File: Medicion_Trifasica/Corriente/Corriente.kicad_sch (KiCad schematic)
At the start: 0 parts

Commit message: Se agrego el circuito de medicion de corriente
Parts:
- added J1: Conn_01x01_Pin, symbol Connector:Conn_01x01_Pin
- added R1: 22k, symbol Device:R
- added R2: 10k, symbol Device:R
- added U1: ACS725xLCTR-20AB, Package_SO:SOIC-8_3.9x4.9mm_P1.27mm, symbol Sensor_Current:ACS725xLCTR-20AB
- added U2: TL082, symbol Amplifier_Operational:TL082
- added U3: ADR4533, Package_SO:SOIC-8_3.9x4.9mm_P1.27mm, symbol Reference_Voltage:ADR4533
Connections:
- new net: J1.1 (Pin_1), U2.1, U2.2 (-)
- new net: R1.1, U1.7 (VIOUT)
- new net: R1.2, R2.1, U2.3 (+)
- new net: U1.1 (IP+), U1.2 (IP+)
- new net: U1.3 (IP-), U1.4 (IP-)
- new net: U1.8 (VCC), U3.6 (OUT)
- new net +9V: U3.2 (IN)
- new net GND: R2.2, U1.5 (GND), U3.4 (GND)

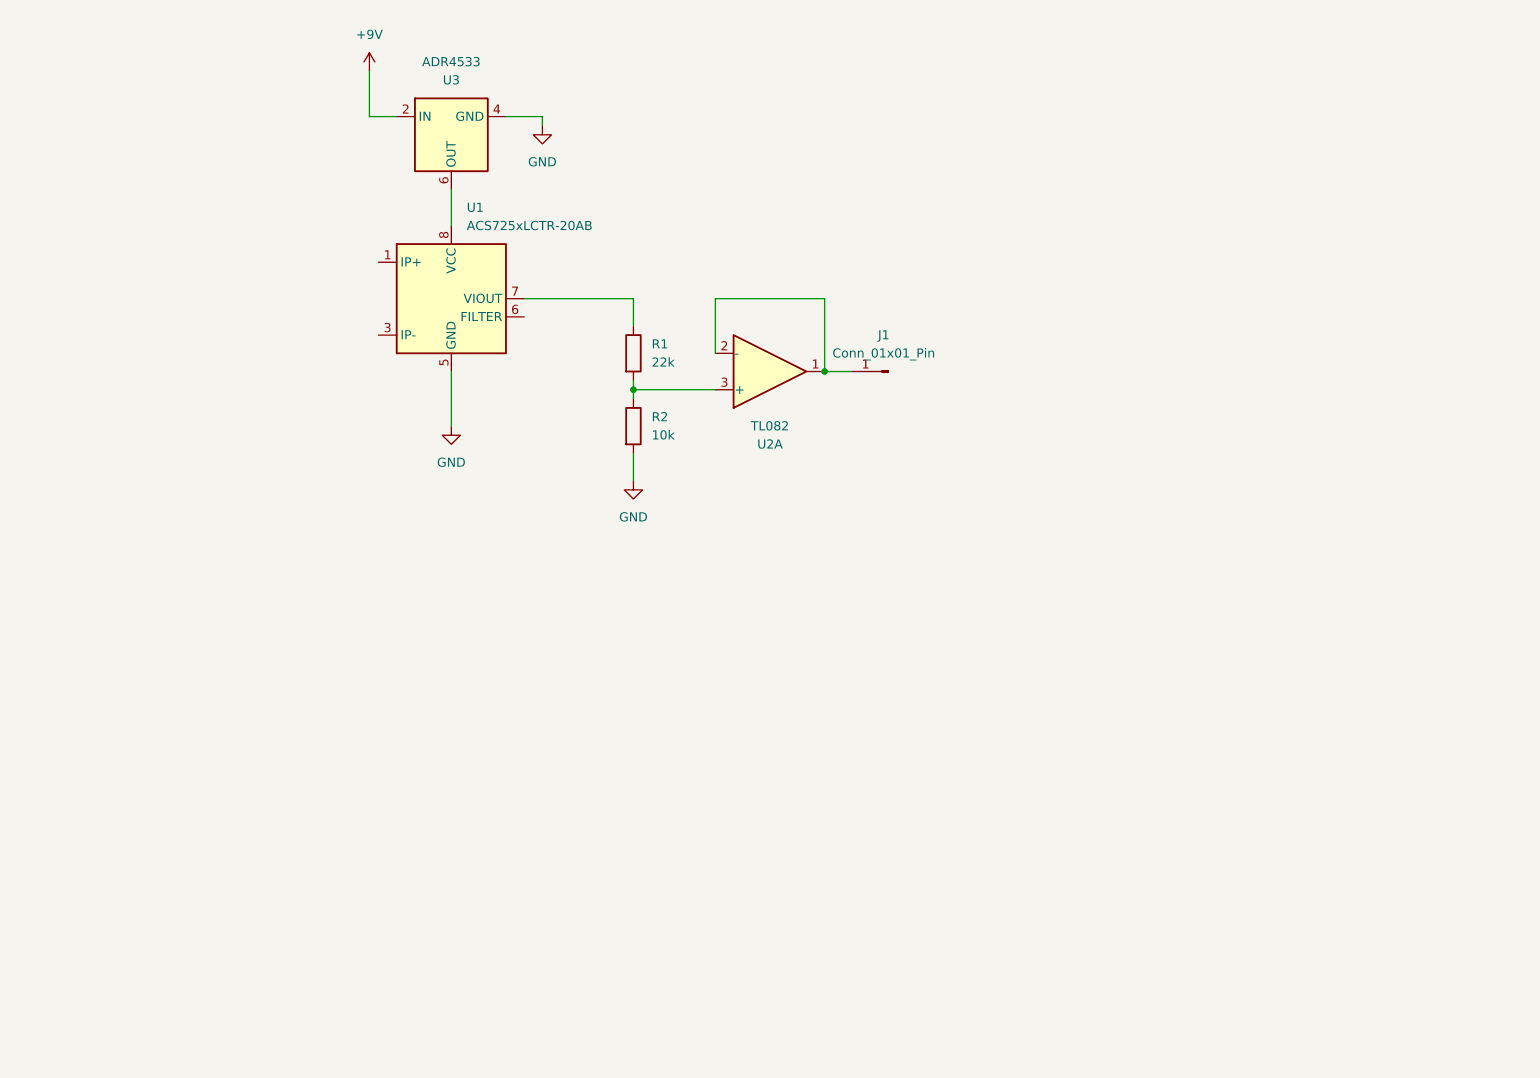
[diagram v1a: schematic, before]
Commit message: Modificaciones finales a los circuitos de medicion de corriente y tension
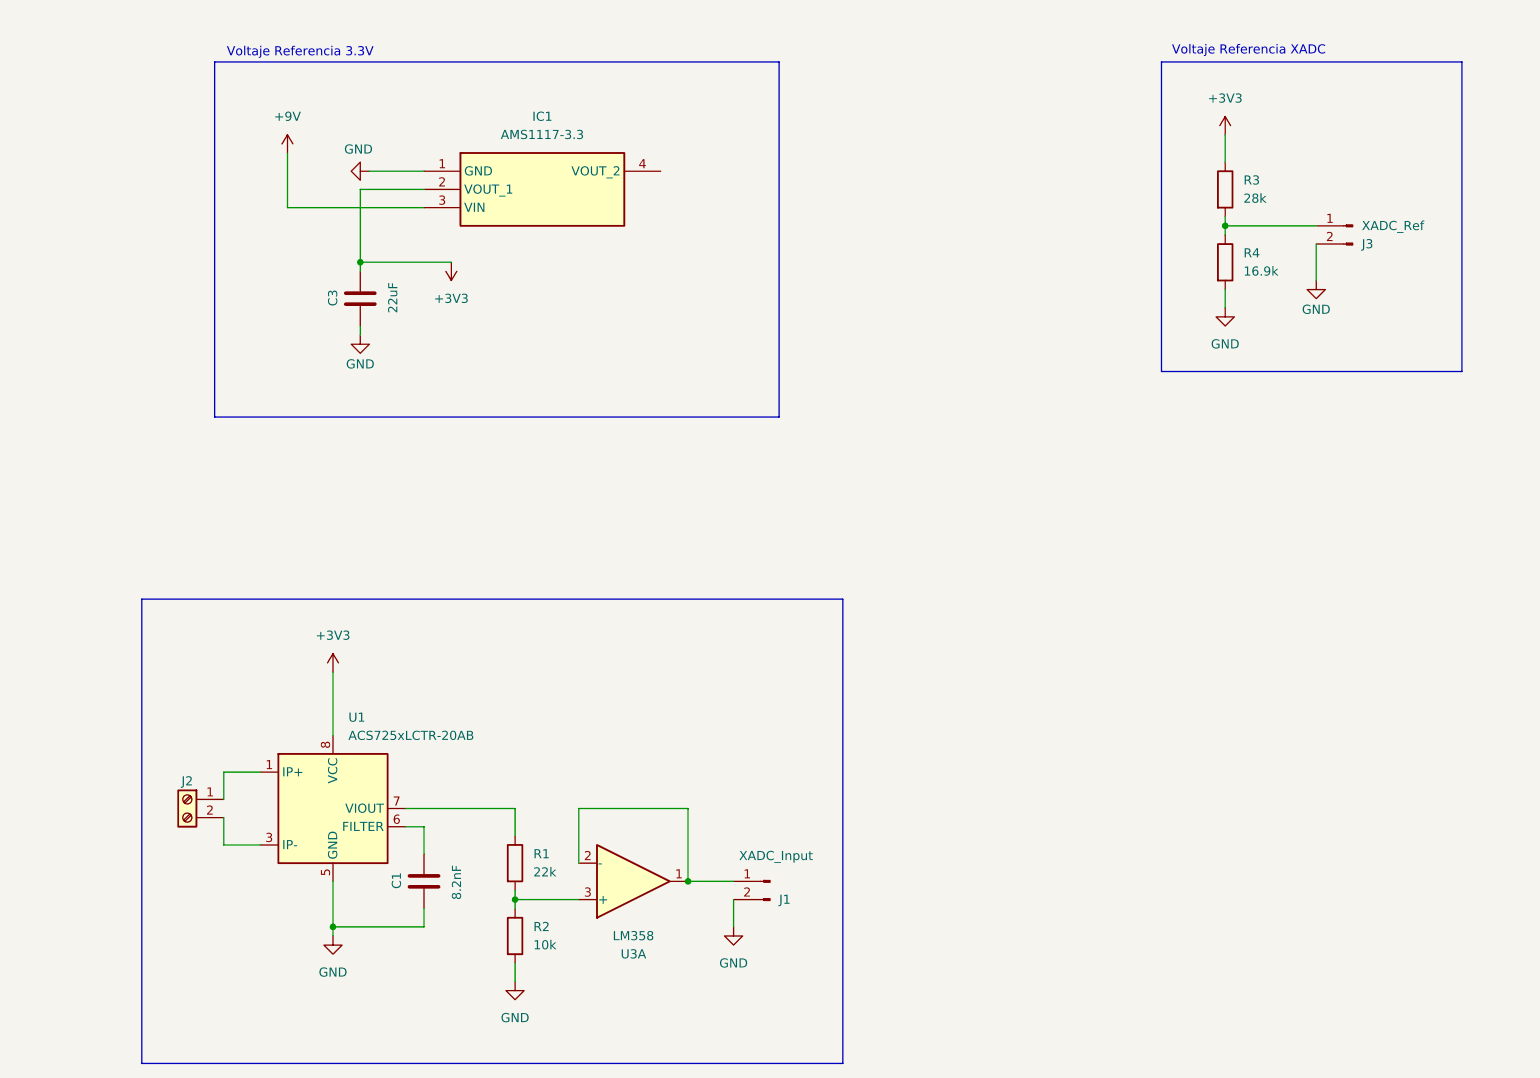
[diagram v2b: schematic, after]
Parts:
- removed J1: Conn_01x01_Pin, symbol Connector:Conn_01x01_Pin
- removed U2: TL082, symbol Amplifier_Operational:TL082
- removed U3: ADR4533, Package_SO:SOIC-8_3.9x4.9mm_P1.27mm, symbol Reference_Voltage:ADR4533
- added C1: 8.2nF, symbol Device:C
- added C3: 22uF, symbol Device:C
- added IC1: AMS1117-3.3, SOT229P700X180-4N, symbol SamacSys_Parts:AMS1117-3.3
- added J1: XADC_Input, symbol Connector:Conn_01x02_Pin
- added J2: Screw_Terminal_01x02, symbol Connector:Screw_Terminal_01x02
- added J3: XADC_Ref, symbol Connector:Conn_01x02_Pin
- added R3: 28k, symbol Device:R
- added R4: 16.9k, symbol Device:R
- added U3: LM358, symbol Amplifier_Operational:LM358
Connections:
- net +9V: now also IC1.3 (VIN)
- net GND: now also C1.1, C3.1, IC1.1 (GND), J1.2 (Pin_2), J3.2 (Pin_2), R4.2
- net at R1.2, R2.1: now also U3.3 (+)
- net at U1.1 (IP+), U1.2 (IP+): now also J2.1 (Pin_1)
- net at U1.3 (IP-), U1.4 (IP-): now also J2.2 (Pin_2)
- net at U1.6 (FILTER): now also C1.2
- net +3V3: now reaches U1.8 (VCC)
- net +3V3: now also C3.2, IC1.2 (VOUT_1), R3.1
- new net: J3.1 (Pin_1), R3.2, R4.1
- new net: J1.1 (Pin_1), U3.1, U3.2 (-)
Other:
- note added: "Voltaje Referencia 3.3V"
- note added: "Voltaje Referencia XADC"
- company: (none) -> U.N.R
- title: (none) -> Medicion de Corriente
- moved on the sheet: R1, R2, U1

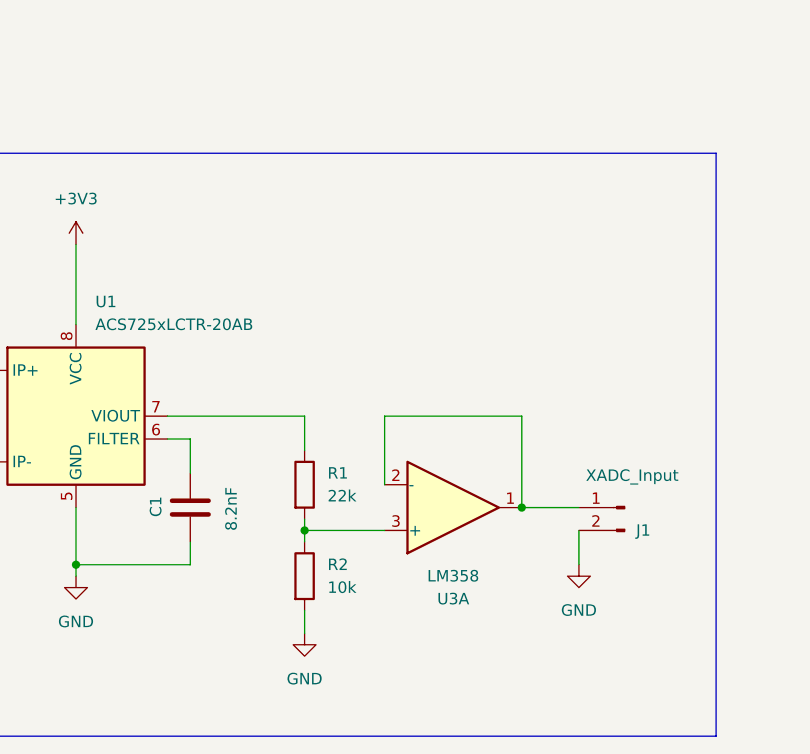
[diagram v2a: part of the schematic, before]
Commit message: Se crearon los esquematicos de los circuitos, y sus footprints
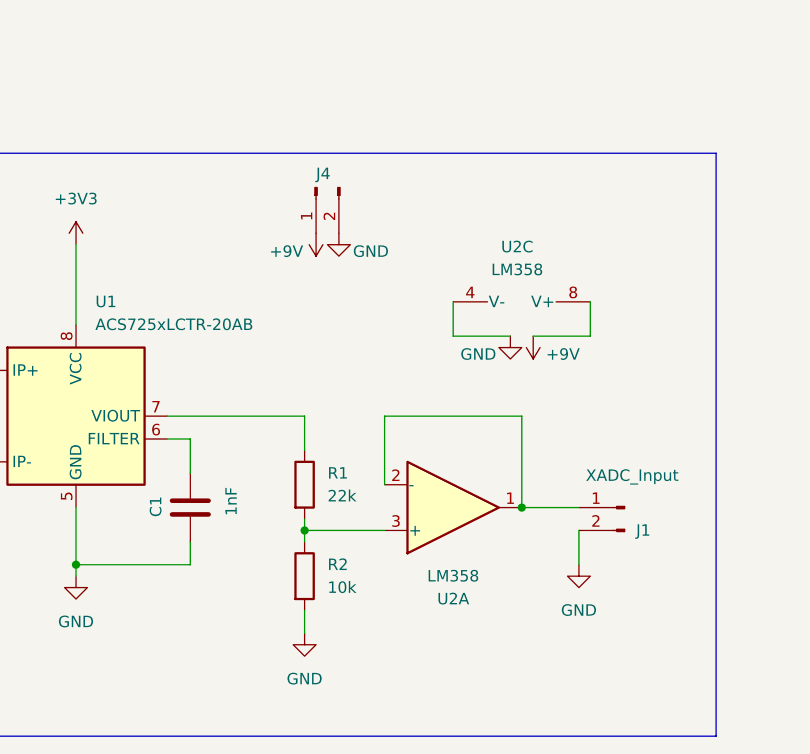
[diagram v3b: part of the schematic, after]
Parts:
- added J4: XADC_Input, Connector_PinHeader_2.54mm:PinHeader_1x02_P2.54mm_Vertical, symbol Connector:Conn_01x02_Pin
- added unit 3 of U2
- C1: value 8.2nF -> 1nF; footprint (none) -> Capacitor_SMD:C_01005_0402Metric_Pad0.57x0.30mm_HandSolder
- C3: footprint (none) -> Capacitor_SMD:C_1206_3216Metric_Pad1.33x1.80mm_HandSolder
- IC1: footprint SOT229P700X180-4N -> SamacSys_Parts:SOT229P700X180-4N
- J1, J3: footprint (none) -> Connector_PinHeader_2.54mm:PinHeader_2x01_P2.54mm_Horizontal
- J2: footprint (none) -> TerminalBlock:TerminalBlock_bornier-2_P5.08mm
- R1, R2, R3, R4: footprint (none) -> Resistor_SMD:R_0805_2012Metric_Pad1.20x1.40mm_HandSolder
- U2: renamed from U3; footprint (none) -> Package_SO:SOIC-8_3.9x4.9mm_P1.27mm
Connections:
- net +9V: now also J4.1 (Pin_1), U2.8 (V+)
- net GND: now also J4.2 (Pin_2), U2.4 (V-)

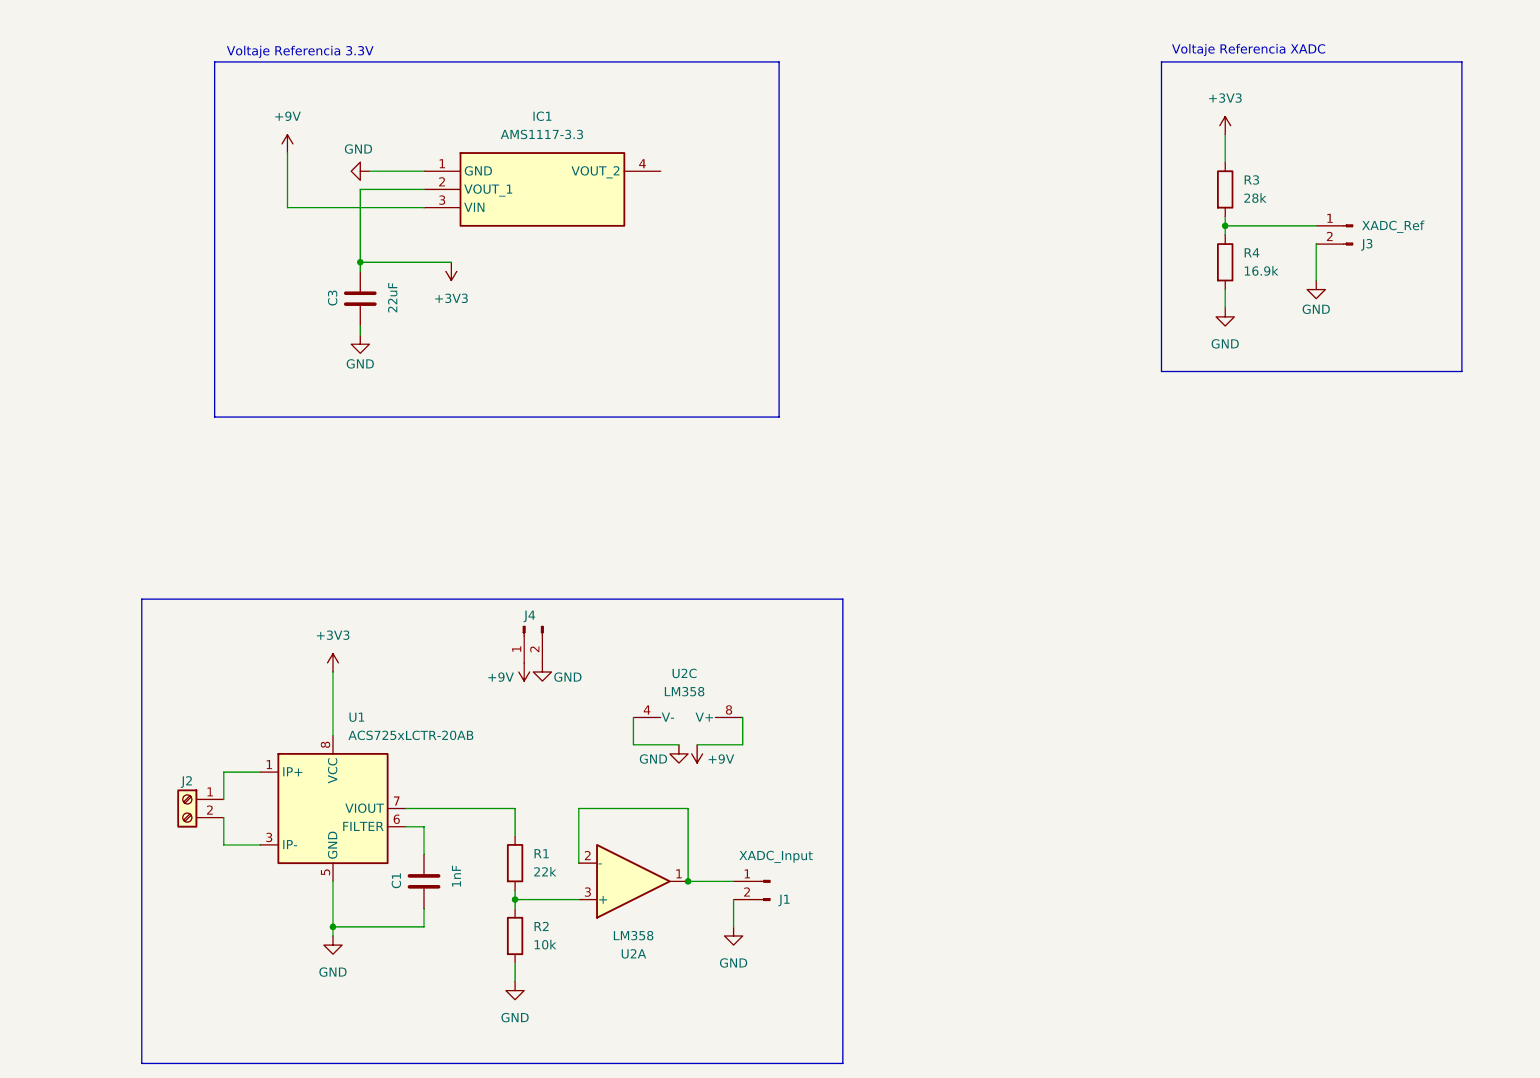
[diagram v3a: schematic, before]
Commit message: Correciones PCBs
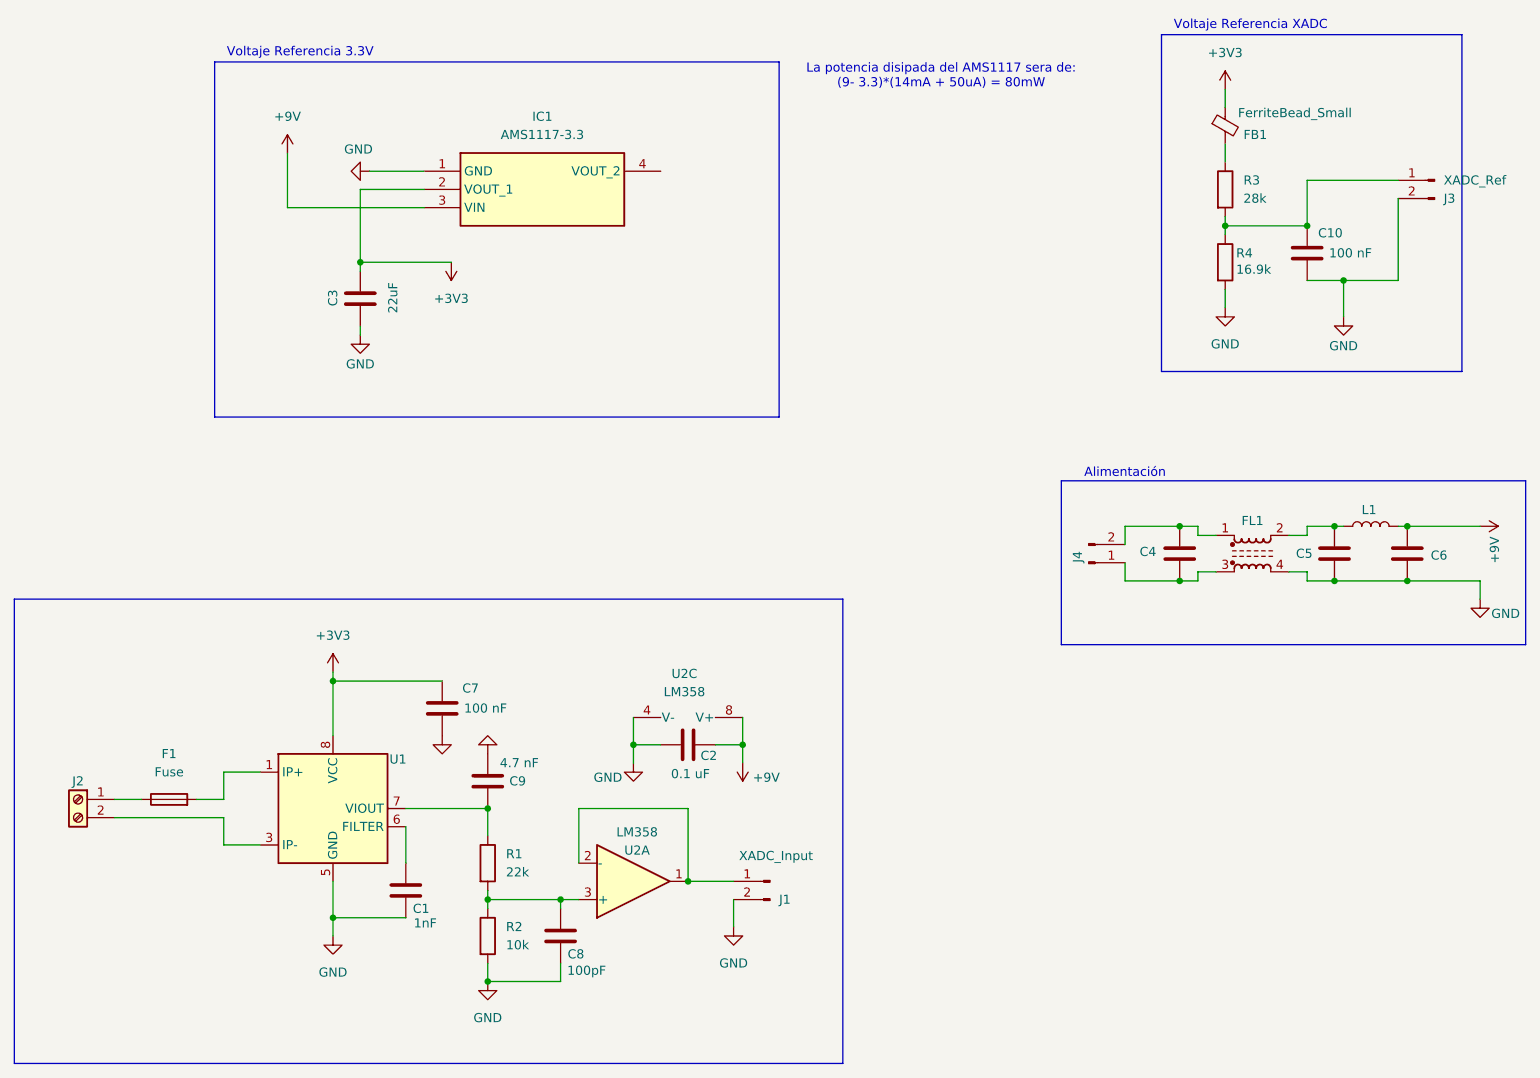
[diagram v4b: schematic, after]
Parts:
- added C10, C5, C6, C7: 100 nF, Capacitor_SMD:C_1206_3216Metric_Pad1.33x1.80mm_HandSolder, symbol Device:C
- added C2: 0.1 uF, Capacitor_SMD:C_1206_3216Metric_Pad1.33x1.80mm_HandSolder, symbol Device:C
- added C4: 470 uF, Capacitor_SMD:C_1206_3216Metric_Pad1.33x1.80mm_HandSolder, symbol Device:C
- added C8: 100pF, Capacitor_SMD:C_01005_0402Metric_Pad0.57x0.30mm_HandSolder, symbol Device:C
- added C9: 4.7 nF, Capacitor_SMD:C_01005_0402Metric_Pad0.57x0.30mm_HandSolder, symbol Device:C
- added F1: Fuse, Fuse:FuseHolder_Blade_ATO_Littelfuse_FLR_178.6165, symbol Device:Fuse
- added FB1: FerriteBead_Small, Inductor_SMD:L_0603_1608Metric, symbol Device:FerriteBead_Small
- added FL1: Choke_CommonMode_FerriteCore_1234, Inductor_THT:Choke_EPCOS_B82722A, symbol Filter:Choke_CommonMode_FerriteCore_1234
- added L1: L, Inductor_SMD:L_7.3x7.3_H3.5, symbol Device:L
- J4: value XADC_Input -> POWER
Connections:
- net +3V3: now also C7.1, FB1.1; no longer R3.1
- net +9V: now also C2.2, C6.2, L1.2; no longer J4.1 (Pin_1)
- net GND: now also C10.2, C2.1, C5.1, C6.1, C7.2, C8.1, C9.2, FL1.4; no longer J4.2 (Pin_2)
- net at J3.1 (Pin_1), R3.2, R4.1: now also C10.1
- net at R1.1, U1.7 (VIOUT): now also C9.1
- net at R1.2, R2.1, U2.3 (+): now also C8.2
- net at U1.1 (IP+), U1.2 (IP+): now also F1.2; no longer J2.1 (Pin_1)
- new net: FB1.2, R3.1
- new net: C5.2, FL1.2, L1.1
- new net: C4.2, FL1.3, J4.1 (Pin_1)
- new net: C4.1, FL1.1, J4.2 (Pin_2)
- new net: F1.1, J2.1 (Pin_1)
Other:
- note added: "Alimentación"
- note added: "La potencia disipada del AMS1117 sera de: (9- 3.3)*(14mA + 50uA) = 80mW"
- moved on the sheet: C1, J2, J3, J4, R1, R2
